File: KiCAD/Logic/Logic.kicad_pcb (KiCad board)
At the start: 4 copper layers, 85.9 x 50 mm, 136 parts, among them IC1 TPS63020DSJR, IC2 BQ24075TRGTT, IC3 PN5321A3HN_C106,55, IC4 W25Q32JVSNIQ, J1 JST SH Con, J2 Conn_01x03_Pin, J3 Display Connector, J4 UJ20-C-H-G-MSMT-4B-P16-TR, J5 Battery Conenctor, Q1 BSS84AK,215, Q3 NX7002AKVL, SW1 SW_Push, SW2 RUN, SW3 BOOTSEL, SW4 A_BTN, SW5 B_BTN, U1 RP2040, U2 BQ27441DRZR-G1A, Y1 27M12, Y2 12M

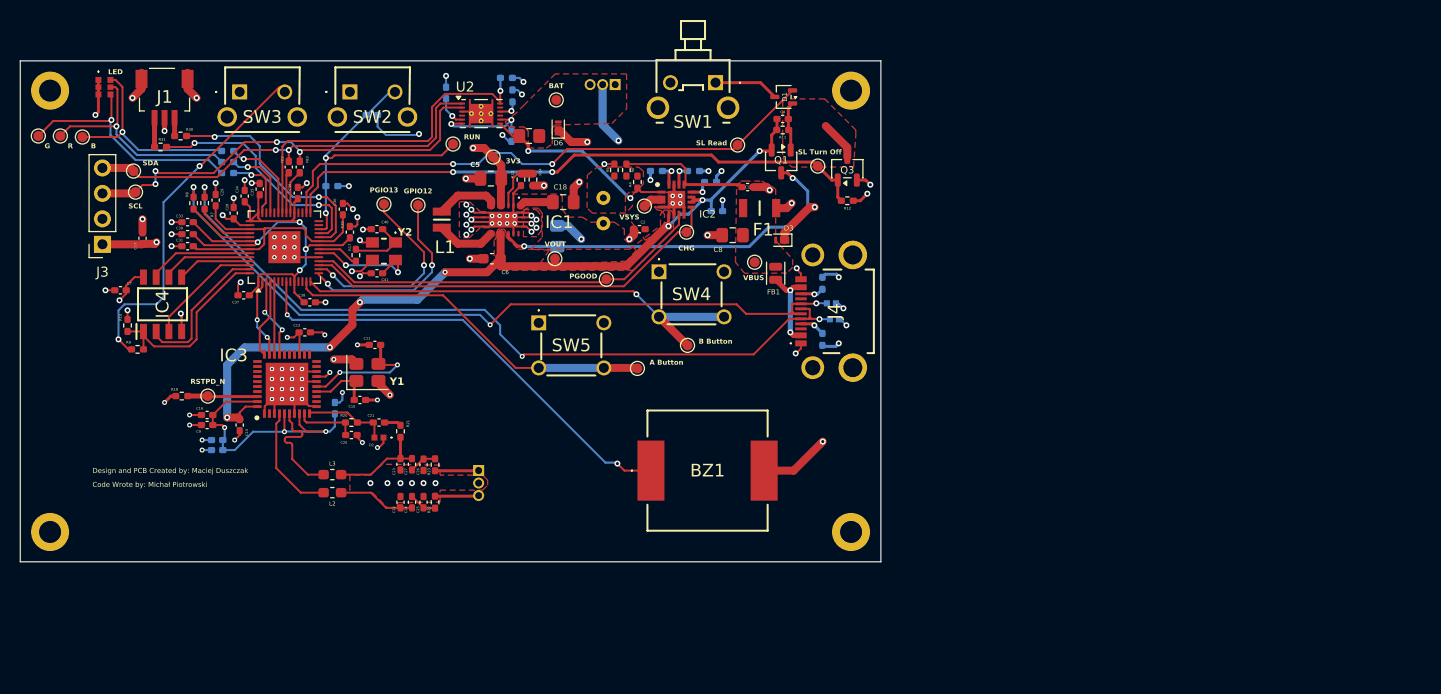
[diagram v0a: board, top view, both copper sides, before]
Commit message: Corrected wrong battery footprint orientation
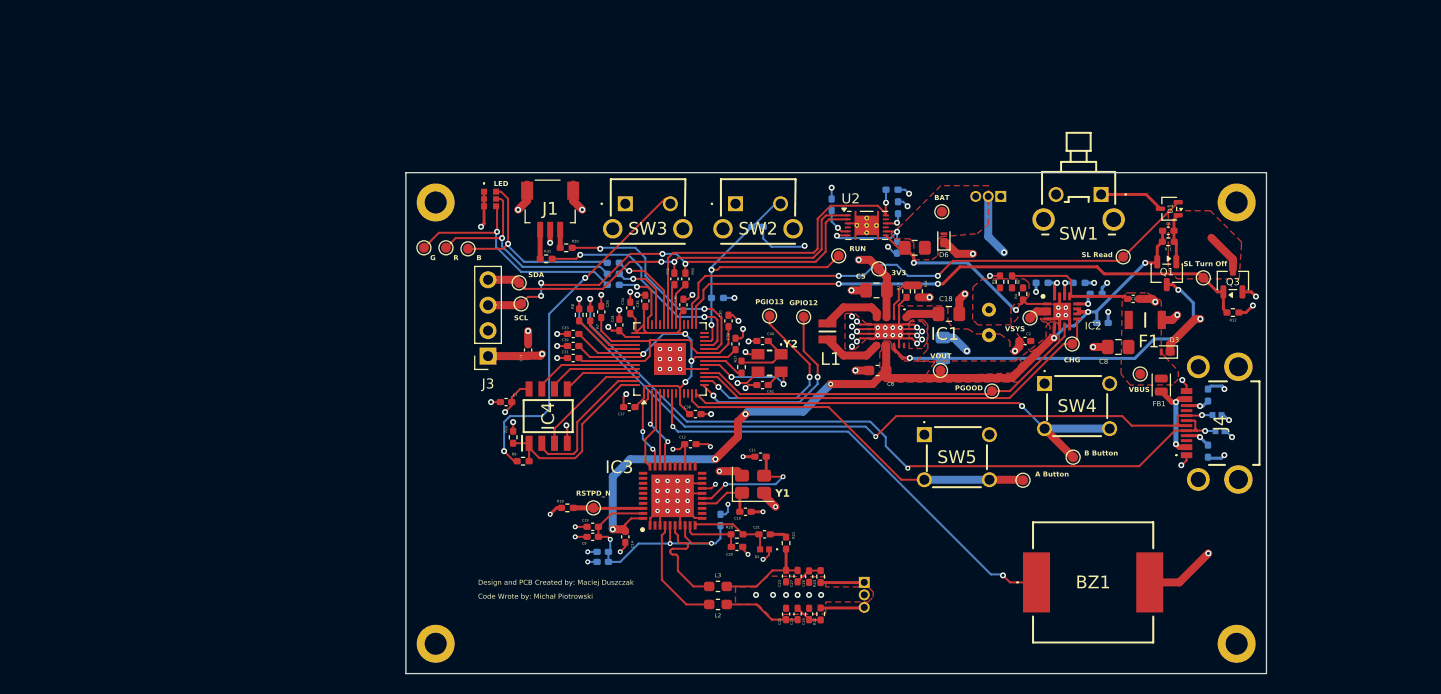
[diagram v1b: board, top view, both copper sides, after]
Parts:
- moved A Button 40.1 mm to (190.9, 91.2)
- moved C34 40.1 mm to (151.7, 74.0)
- moved C35 40.1 mm to (153.2, 73.3)
- moved C4 40.1 mm to (205.4, 66.3)
- moved C44 40.1 mm to (178.3, 68.0)
- moved C5 40.1 mm to (176.2, 72.2)
- moved D5 40.1 mm to (210.2, 84.7)
- moved FB1 40.1 mm to (204.7, 81.7)
- moved J5 40.1 mm to (188.7, 62.9)
- moved R 40.1 mm to (133.3, 68.0)
- moved R2 40.1 mm to (192.8, 71.5)
- moved R30 40.1 mm to (145.3, 68.0)
- moved R7 40.1 mm to (147.7, 74.7)
- moved SL Turn Off 40.1 mm to (208.9, 71.0)
- moved SW1 40.1 mm to (198.7, 62.7)
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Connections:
- J5 pad 1: /Battery Gauge/BAT -> unconnected-(J5-Pin_1-Pad1)
- J5 pad 3: unconnected-(J5-Pin_3-Pad3) -> /Battery Gauge/BAT

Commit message: Added everything for ordering
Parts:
- C18, C45: footprint Capacitor_SMD:C_0805_2012Metric_Pad1.18x1.45mm_HandSolder -> Capacitor_SMD:C_0402_1005Metric_Pad0.74x0.62mm_HandSolder
- R1: value 46k8 -> 46k4
- moved C18 18.2 mm to (198.8, 64.8)
- moved C13 18.1 mm to (156.9, 68.7)
- moved C23 18.1 mm to (182.6, 91.3)
- moved C28 18.1 mm to (166.0, 66.2)
- moved C31 18.1 mm to (161.4, 69.5)
- moved C36 18.1 mm to (172.4, 64.2)
- moved C6 18.1 mm to (191.8, 70.8)
- moved D6 18.1 mm to (198.4, 57.7)
- moved F1 18.1 mm to (218.5, 65.7)
- moved J2 18.1 mm to (190.4, 91.9)
- moved J3 18.1 mm to (152.9, 69.3)
- moved J4 18.1 mm to (226.2, 76.0)
- moved Q3 18.1 mm to (227.2, 61.8)
- moved R16 18.1 mm to (224.7, 73.2)
- moved R24 18.1 mm to (165.4, 62.2)
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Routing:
- net /Buck-Boost/IN: track 88.1 -> 88.9 mm
- net GND: track 152.9 -> 152.4 mm
